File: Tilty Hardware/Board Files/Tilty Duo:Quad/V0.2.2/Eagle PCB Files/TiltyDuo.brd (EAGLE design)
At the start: 38.1 x 50.8 mm, 38 parts, among them U1 TEENSY_3.0_OUTER-PINS28-DIP_S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, U2 HC-09_BREAKOUT, U3 MPL3115A2LGA8, U4 LM2931, U5 MPU-6050, U6 HMC5883LSMD

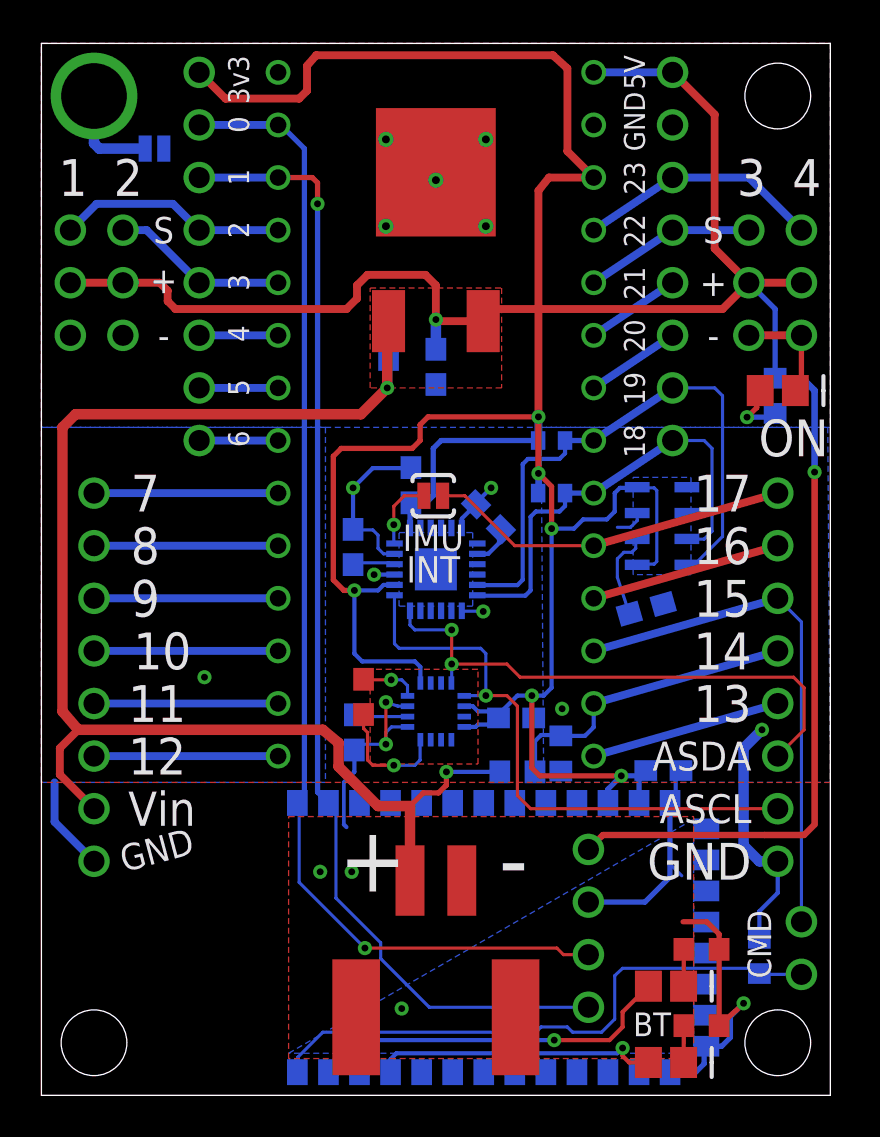
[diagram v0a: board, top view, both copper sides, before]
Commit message: Updated prototype board file
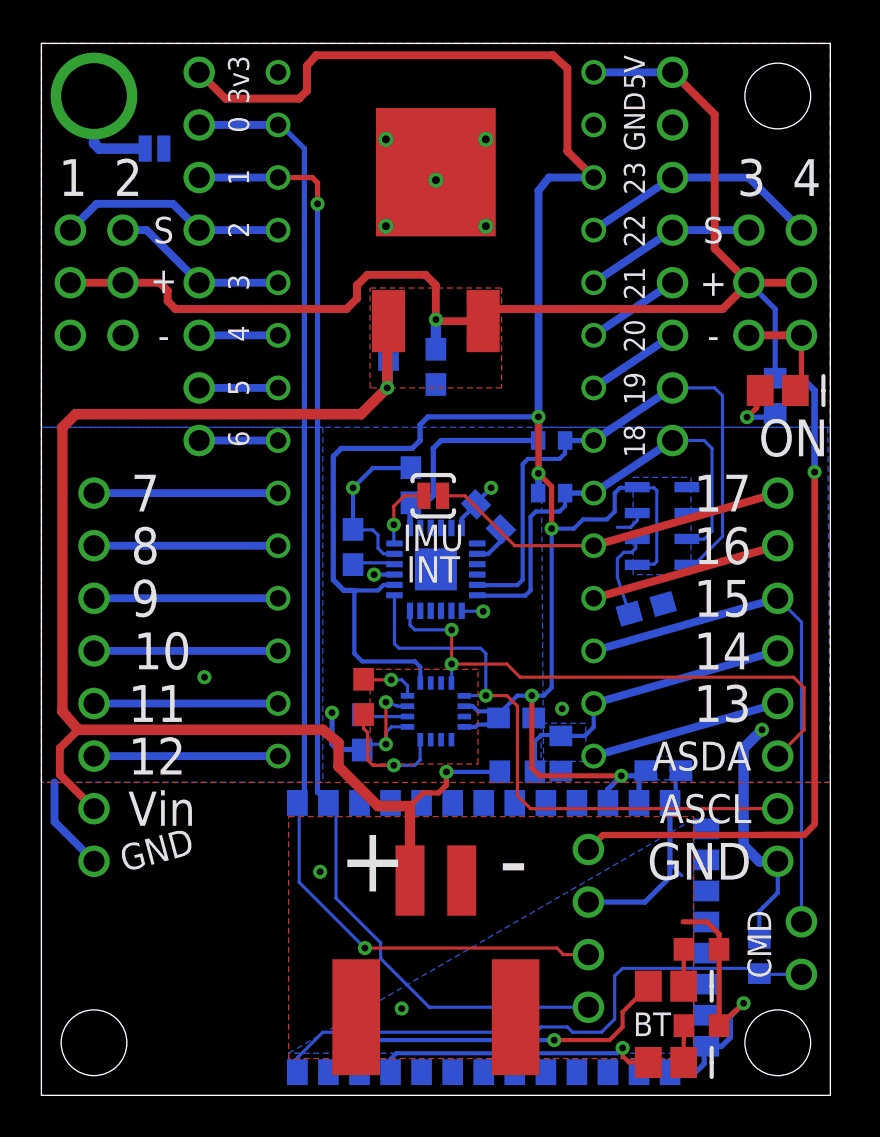
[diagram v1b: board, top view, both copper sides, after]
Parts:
- moved C8 0.38 mm to (15.5, 17.5)
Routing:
- net GND: track 71.5 -> 70.5 mm
- net TEENSY_3V3: vias 6 -> 5
- added copper zone on layer 16, net N$25
- added copper zone on layer 16, net N$26
- removed copper zone on layer 16, net N$22
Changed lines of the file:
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@@
 <element name="U6" library="SparkFun" package="16LPCC" value="HMC5883LSMD" x="19.05" y="18.542" smashed="yes" rot="MR0"/>
 <element name="C7" library="resistor" package="C0603" value="0.22uF" x="15.5575" y="19.2405" smashed="yes" rot="R90"/>
-<element name="C8" library="resistor" package="C0603" value="4.7uF" x="15.113" y="17.526" smashed="yes" rot="MR270"/>
+<element name="C8" library="resistor" package="C0603" value="4.7uF" x="15.494" y="17.526" smashed="yes" rot="MR270"/>
 <element name="C6" library="resistor" package="C0603" value="0.1uF" x="22.9235" y="18.2245" smashed="yes" rot="MR180">
 <attribute name="RATED_VOLTAGE" value="2" x="22.9235" y="18.2245" size="1.778" layer="28" rot="MR180" display="off"/>
@@
 <polygon width="0.1524" layer="16">
 <vertex x="0" y="32.258"/>
-<vertex x="13.716" y="32.258"/>
-<vertex x="13.716" y="15.113"/>
+<vertex x="13.589" y="32.258"/>
+<vertex x="13.589" y="15.113"/>
 <vertex x="0" y="15.113"/>
 </polygon>
@@
 <vertex x="11.938" y="1.778"/>
 </polygon>
-<via x="14.986" y="10.795" extent="1-16" drill="0.3302"/>
+<via x="14.0335" y="18.4785" extent="1-16" drill="0.3302"/>
 <wire x1="30.568" y1="14.328" x2="30.36" y2="14.12" width="0.254" layer="16"/>
 <via x="16.637" y="16.9545" extent="1-16" drill="0.3302"/>
@@
 <wire x1="16.903" y1="17.792" x2="16.637" y2="17.526" width="0.1524" layer="16"/>
 <wire x1="16.637" y1="16.9545" x2="16.637" y2="17.526" width="0.1524" layer="16"/>
-<wire x1="15.3915" y1="16.9545" x2="15.113" y2="16.676" width="0.1524" layer="16"/>
+<wire x1="15.3915" y1="16.9545" x2="15.494" y2="16.676" width="0.1524" layer="16"/>
 <wire x1="16.637" y1="16.9545" x2="15.3915" y2="16.9545" width="0.1524" layer="16"/>
 <contactref element="JP6" pad="1"/>
@@
 <wire x1="30.6315" y1="14.3915" x2="30.6315" y2="15.4305" width="0.2032" layer="16"/>
 <wire x1="30.6315" y1="15.4305" x2="30.8855" y2="15.6845" width="0.2032" layer="16"/>
-<wire x1="15.113" y1="15.621" x2="14.605" y2="15.113" width="0.2032" layer="16"/>
-<wire x1="14.605" y1="15.113" x2="14.605" y2="13.081" width="0.1778" layer="16"/>
-<wire x1="14.605" y1="13.081" x2="14.732" y2="12.954" width="0.2032" layer="16"/>
-<wire x1="15.113" y1="15.621" x2="15.113" y2="16.676" width="0.2032" layer="16"/>
 <wire x1="20.988959375" y1="28.541040625" x2="20.988959375" y2="28.608959375" width="0.2032" layer="16"/>
 <wire x1="20.988959375" y1="28.608959375" x2="21.717" y2="29.337" width="0.2032" layer="16"/>
@@
 <wire x1="33.274" y1="2.794" x2="33.274" y2="3.81" width="0.254" layer="16"/>
 <wire x1="33.274" y1="3.81" x2="33.909" y2="4.445" width="0.254" layer="16"/>
+<wire x1="14.0335" y1="18.4785" x2="14.0335" y2="16.9545" width="0.254" layer="16"/>
+<wire x1="14.0335" y1="16.9545" x2="14.2875" y2="16.7005" width="0.254" layer="16"/>
+<wire x1="14.2875" y1="16.7005" x2="15.4695" y2="16.7005" width="0.254" layer="16"/>
+<wire x1="15.4695" y1="16.7005" x2="15.494" y2="16.676" width="0.254" layer="16"/>
 </signal>
 <signal name="SCL" class="4">
@@
 <contactref element="C3" pad="1"/>
 <wire x1="21.05" y1="26.15" x2="21.578" y2="26.15" width="0.2032" layer="16"/>
-<wire x1="21.578" y1="26.15" x2="22.098" y2="26.67" width="0.2032" layer="16"/>
-<wire x1="22.098" y1="26.67" x2="22.098" y2="27.2459125" width="0.2032" layer="16"/>
+<wire x1="21.578" y1="26.15" x2="22.225" y2="26.797" width="0.2032" layer="16"/>
+<wire x1="22.225" y1="26.797" x2="22.098" y2="27.2459125" width="0.2032" layer="16"/>
 <wire x1="22.098" y1="27.2459125" x2="22.19104375" y2="27.33895625" width="0.2032" layer="16"/>
 </signal>
@@
 <contactref element="C6" pad="1"/>
 <via x="24.003" y="30.0355" extent="1-16" drill="0.3302"/>
-<wire x1="26.67" y1="44.323" x2="24.511" y2="44.323" width="0.381" layer="1"/>
-<wire x1="24.511" y1="44.323" x2="24.003" y2="43.688" width="0.381" layer="1"/>
-<wire x1="24.003" y1="43.688" x2="24.003" y2="32.766" width="0.381" layer="1"/>
+<wire x1="26.67" y1="44.323" x2="24.511" y2="44.323" width="0.381" layer="16"/>
+<wire x1="24.511" y1="44.323" x2="24.003" y2="43.688" width="0.381" layer="16"/>
+<wire x1="24.003" y1="43.688" x2="24.003" y2="32.766" width="0.381" layer="16"/>
 <via x="24.003" y="32.766" extent="1-16" drill="0.3302"/>
 <wire x1="24.003" y1="32.766" x2="24.003" y2="31.638" width="0.381" layer="16"/>
@@
 <wire x1="24.003" y1="30.0355" x2="24.003" y2="29.098" width="0.3048" layer="16"/>
 <wire x1="24.003" y1="29.098" x2="23.988" y2="29.083" width="0.3048" layer="16"/>
-<via x="15.113" y="24.384" extent="1-16" drill="0.3302"/>
-<wire x1="24.003" y1="32.766" x2="18.669" y2="32.766" width="0.254" layer="1"/>
-<wire x1="18.669" y1="32.766" x2="18.288" y2="32.385" width="0.254" layer="1"/>
-<wire x1="18.288" y1="32.385" x2="18.288" y2="31.623" width="0.254" layer="1"/>
-<wire x1="18.288" y1="31.623" x2="17.907" y2="31.242" width="0.254" layer="1"/>
-<wire x1="17.907" y1="31.242" x2="14.478" y2="31.242" width="0.254" layer="1"/>
-<wire x1="14.478" y1="31.242" x2="14.097" y2="30.861" width="0.254" layer="1"/>
-<wire x1="14.097" y1="30.861" x2="14.097" y2="24.892" width="0.254" layer="1"/>
+<wire x1="24.003" y1="32.766" x2="18.669" y2="32.766" width="0.254" layer="16"/>
+<wire x1="18.669" y1="32.766" x2="18.288" y2="32.385" width="0.254" layer="16"/>
+<wire x1="18.288" y1="32.385" x2="18.288" y2="31.623" width="0.254" layer="16"/>
+<wire x1="18.288" y1="31.623" x2="17.907" y2="31.242" width="0.254" layer="16"/>
+<wire x1="17.907" y1="31.242" x2="14.478" y2="31.242" width="0.254" layer="16"/>
+<wire x1="14.478" y1="31.242" x2="14.097" y2="30.861" width="0.254" layer="16"/>
+<wire x1="14.097" y1="30.861" x2="14.097" y2="24.892" width="0.254" layer="16"/>
 <wire x1="17.05" y1="24.65" x2="16.522" y2="24.65" width="0.2032" layer="16"/>
 <wire x1="16.522" y1="24.65" x2="16.256" y2="24.384" width="0.2032" layer="16"/>
 <wire x1="15.113" y1="24.384" x2="16.256" y2="24.384" width="0.2032" layer="16"/>
-<wire x1="14.097" y1="24.892" x2="14.605" y2="24.384" width="0.254" layer="1"/>
-<wire x1="14.605" y1="24.384" x2="15.113" y2="24.384" width="0.254" layer="1"/>
+<wire x1="14.097" y1="24.892" x2="14.605" y2="24.384" width="0.254" layer="16"/>
+<wire x1="14.605" y1="24.384" x2="15.113" y2="24.384" width="0.254" layer="16"/>
 <wire x1="18.3" y1="19.912" x2="18.3" y2="20.689" width="0.2032" layer="16"/>
 <wire x1="18.3" y1="20.689" x2="18.034" y2="20.955" width="0.2032" layer="16"/>
@@
 <contactref element="C8" pad="1"/>
 <wire x1="17.68" y1="18.292" x2="15.197" y2="18.292" width="0.1524" layer="16"/>
-<wire x1="15.197" y1="18.292" x2="15.113" y2="18.376" width="0.1524" layer="16"/>
+<wire x1="15.197" y1="18.292" x2="15.494" y2="18.376" width="0.1524" layer="16"/>
 </signal>
 <signal name="N$16">
@@
 </polygon>
 </signal>
-<signal name="N$22">
-<polygon width="0.1524" layer="16" pour="cutout">
-<vertex x="17.272" y="27.178"/>
-<vertex x="20.828" y="27.178"/>
-<vertex x="20.828" y="23.622"/>
-<vertex x="17.272" y="23.622"/>
-</polygon>
-</signal>
 <signal name="N$21">
 <contactref element="U3" pad="2"/>
@@
 <wire x1="31.0125" y1="1.5875" x2="31.027" y2="3.3655" width="0.2032" layer="1"/>
 </signal>
+<signal name="N$25">
+<polygon width="0.1524" layer="16" pour="cutout">
+<vertex x="29.718" y="15.24"/>
+<vertex x="29.718" y="16.383"/>
+<vertex x="30.353" y="16.383"/>
+<vertex x="30.353" y="15.24"/>
+</polygon>
+</signal>
+<signal name="N$26">
+<polygon width="0.1524" layer="16" pour="cutout">
+<vertex x="24.13" y="16.129"/>
+<vertex x="26.289" y="16.129"/>
+<vertex x="26.289" y="17.9705"/>
+<vertex x="24.13" y="17.9705"/>
+</polygon>
+</signal>
 </signals>

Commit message: Added 1kB EEPROM chip to V0.2.2 board
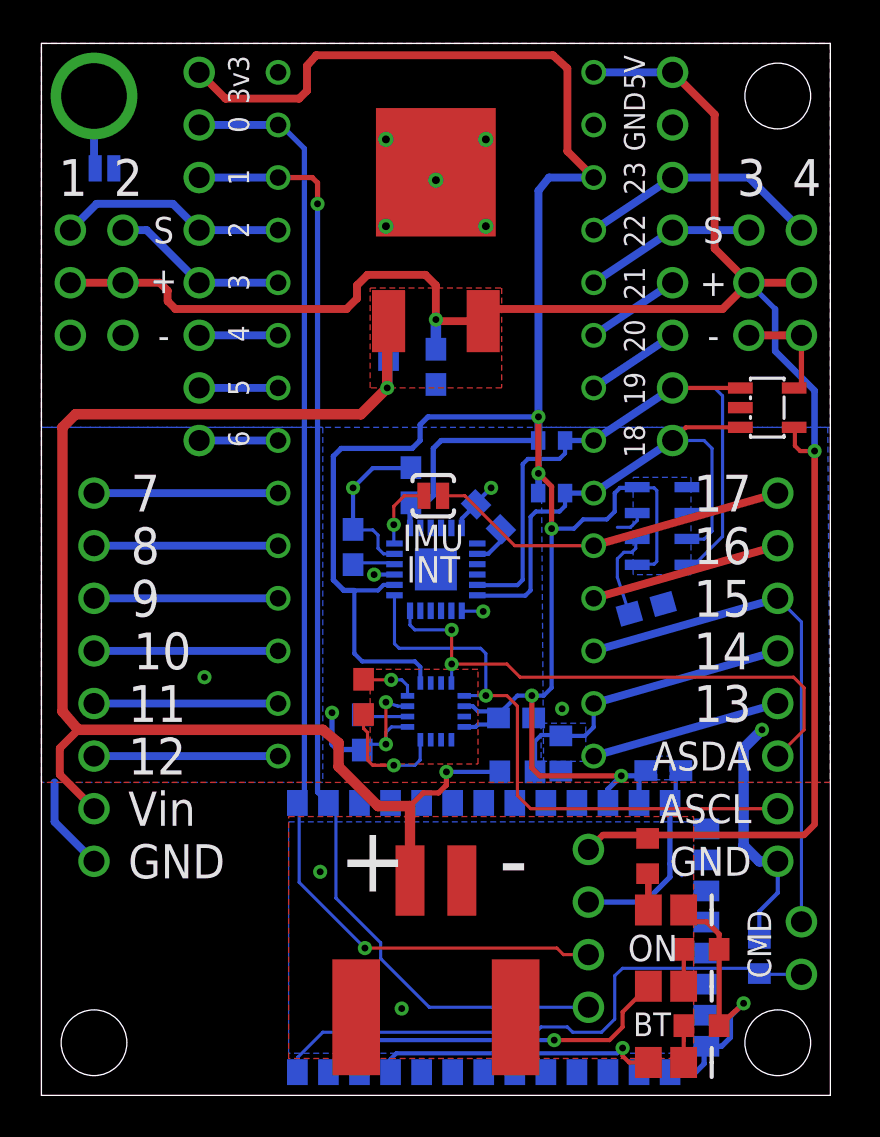
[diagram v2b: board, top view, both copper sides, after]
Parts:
- added U7: 24LC08BT, microchip:SOT23-5L
- moved D2 25.7 mm to (30.2, 8.95)
- moved R4 23.1 mm to (29.3, 11.6), flipped to the top
- moved SJ1 2.59 mm to (3.05, 44.8)
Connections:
- net 5V: now also U7.4
- net GND: now also U7.2, U7.5
- net SCL: now also U7.1
- net SDA: now also U7.3
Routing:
- net SDA: track 22.1 -> 25.7 mm
- net SCL: track 28.4 -> 31.7 mm
- net 5V: track 96.4 -> 97.8 mm
- net CHASSIS_GND: track 4.86 -> 3.52 mm
- net N$17: track 2.99 -> 1.79 mm, vias 1 -> 0

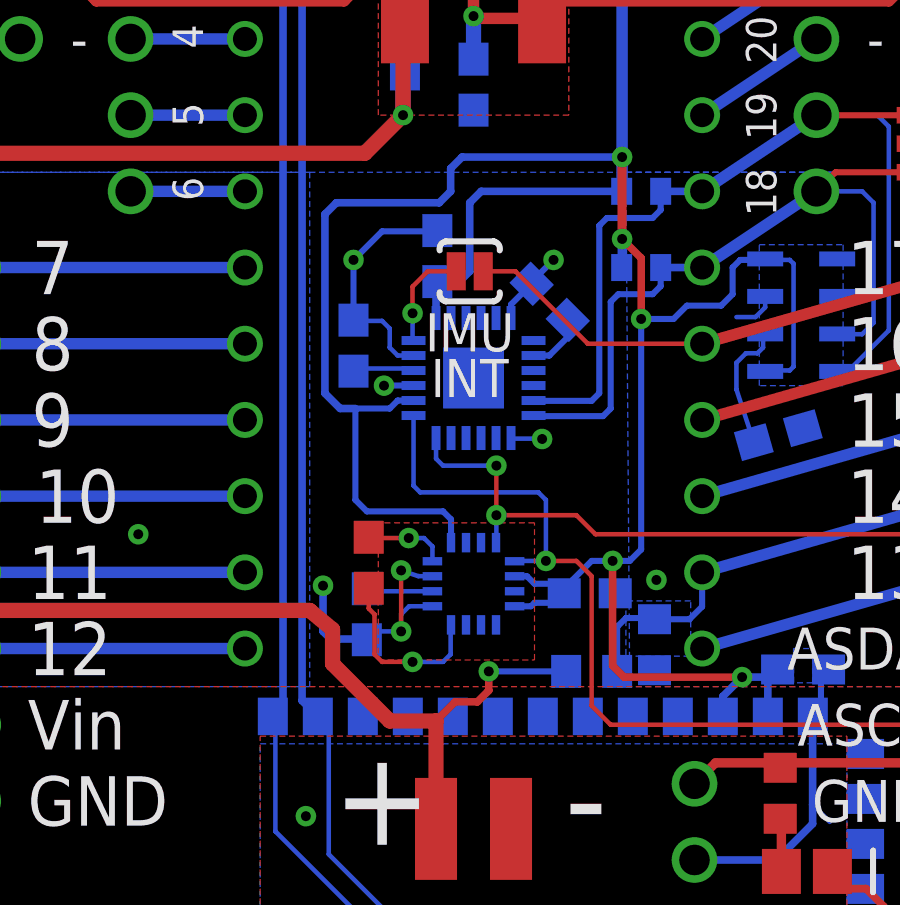
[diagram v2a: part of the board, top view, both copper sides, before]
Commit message: V 0.2.2 of the board and bluetoth arduino libraries updated
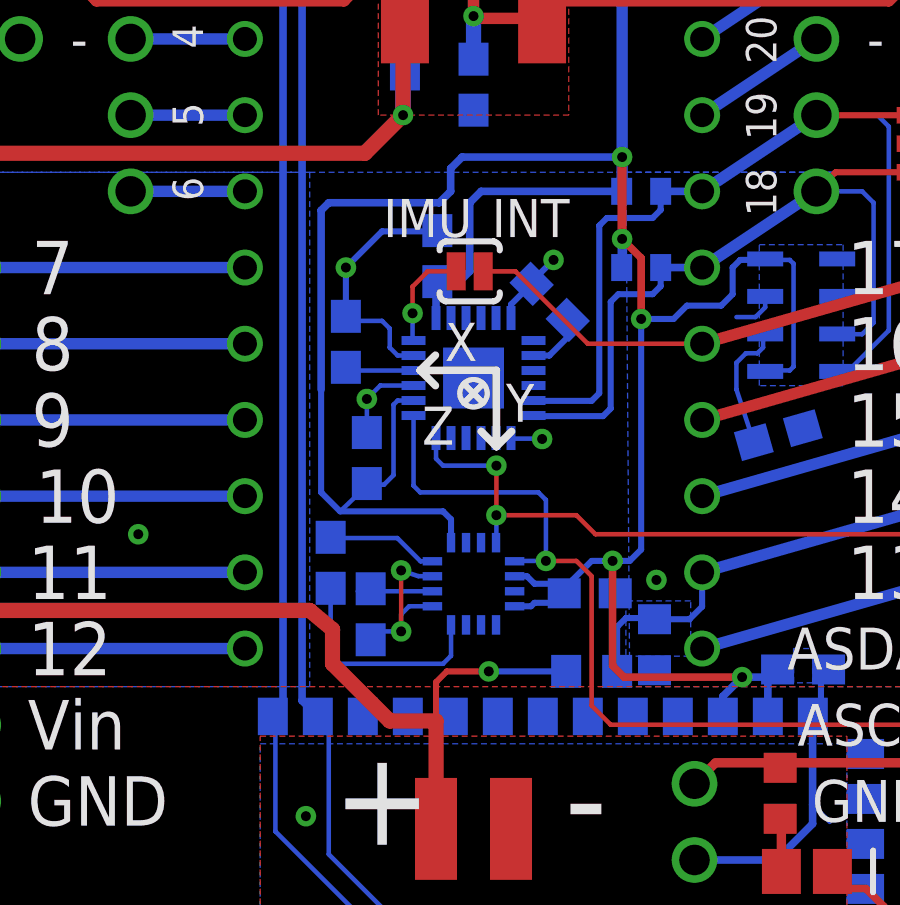
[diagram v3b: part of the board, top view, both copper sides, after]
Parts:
- added C11: 0.1uF, resistor:C0603
- C5, C6, C9: value 0.1uF -> 1uF
- moved C7 1.27 mm to (14.3, 19.2), flipped to the bottom
- moved C1 0.28 mm to (14.8, 26.6)
- moved C8 0.13 mm to (15.6, 17.5)
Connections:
- net GND: now also C11.1
- net TEENSY_3V3: now also C11.2
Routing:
- net TEENSY_3V3: track 123.5 -> 127.3 mm
- net N$5: track 6.01 -> 7.56 mm, vias 1 -> 0
- net N$6: track 2.74 -> 3.72 mm, vias 1 -> 0
- net GND: track 70.1 -> 69.3 mm, vias 18 -> 17
- removed copper zone on layer 1, net N$4
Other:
- board text added: "X"
- board text added: "Y"
- board text added: "Z"

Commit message: Software and Hardware update
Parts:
- added C12: 1uF, resistor:C0603
- added SJ2, SJ3: (no value), SparkFun-Passives:SJ_3
- C6: value 1uF -> 0.1uF
- moved C4 2.44 mm to (15.6, 34.2), turned to 270 degrees
- moved C5 1.66 mm to (20.4, 34.3), turned to 0 degrees
- moved U3 0.13 mm to (30.0, 27.4)
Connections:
- new net POW_I/O1: JP3.3, JP3.4, SJ2.2
- new net POW_I/O2: JP7.3, JP7.4, SJ3.2
- net 5V: now also SJ2.1, SJ3.1; no longer JP3.3, JP3.4, JP7.3, JP7.4
- net GND: now also C12.1
- net TEENSY_3V3: now also C12.2, SJ2.3, SJ3.3
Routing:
- net 5V: track 97.8 -> 81.3 mm
- net POW_I/O2: track 0.00 -> 16.2 mm, vias 0 -> 1
- net POW_I/O1: track 0.00 -> 16.2 mm, vias 0 -> 1
- net TEENSY_3V3: track 127.3 -> 135.2 mm
- net GND: track 69.3 -> 66.9 mm, vias 17 -> 21
- net AUXDA: track 26.7 -> 28.3 mm
- added copper zone on layer 16, net N$4
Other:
- board text added: "5v"
